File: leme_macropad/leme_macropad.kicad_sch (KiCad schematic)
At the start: 41 parts, among them J1 USB_C_Receptacle_USB2.0_16P, U1 SRV05-4HTG-D, U2 NCP1117-3.3_SOT223

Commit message: Changes resistors and capacitors to 0402
This should make it much easier to route things and to comply with the
signal integrity needs of some parts of the circuit.
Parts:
- C1, C2: footprint Capacitor_SMD:C_0603_1608Metric_Pad1.08x0.95mm_HandSolder -> Capacitor_SMD:C_0402_1005Metric_Pad0.74x0.62mm_HandSolder
- R1, R2: footprint Resistor_SMD:R_0603_1608Metric_Pad0.98x0.95mm_HandSolder -> Resistor_SMD:R_0402_1005Metric_Pad0.72x0.64mm_HandSolder
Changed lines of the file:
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@@
 			)
 		)
-		(property "Footprint" "Resistor_SMD:R_0603_1608Metric_Pad0.98x0.95mm_HandSolder"
+		(property "Footprint" "Resistor_SMD:R_0402_1005Metric_Pad0.72x0.64mm_HandSolder"
 			(at 54.61 43.18 0)
 			(effects
@@
 			)
 		)
-		(property "Footprint" "Capacitor_SMD:C_0603_1608Metric_Pad1.08x0.95mm_HandSolder"
+		(property "Footprint" "Capacitor_SMD:C_0402_1005Metric_Pad0.74x0.62mm_HandSolder"
 			(at 156.21 38.1 0)
 			(effects
@@
 			)
 		)
-		(property "Footprint" "Capacitor_SMD:C_0603_1608Metric_Pad1.08x0.95mm_HandSolder"
+		(property "Footprint" "Capacitor_SMD:C_0402_1005Metric_Pad0.74x0.62mm_HandSolder"
 			(at 125.73 38.1 0)
 			(effects
@@
 			)
 		)
-		(property "Footprint" "Resistor_SMD:R_0603_1608Metric_Pad0.98x0.95mm_HandSolder"
+		(property "Footprint" "Resistor_SMD:R_0402_1005Metric_Pad0.72x0.64mm_HandSolder"
 			(at 54.61 40.64 0)
 			(effects

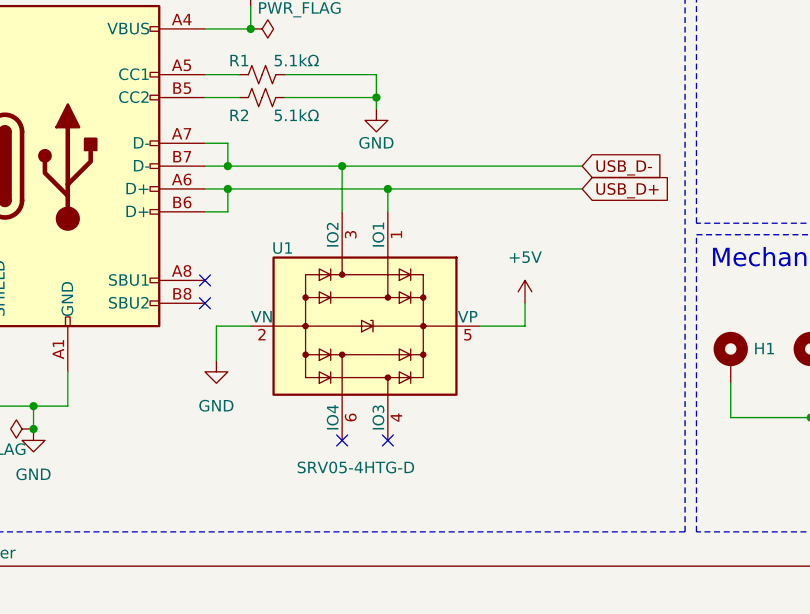
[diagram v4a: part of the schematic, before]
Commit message: Swaps USB pins on SRV05 to make routing easier
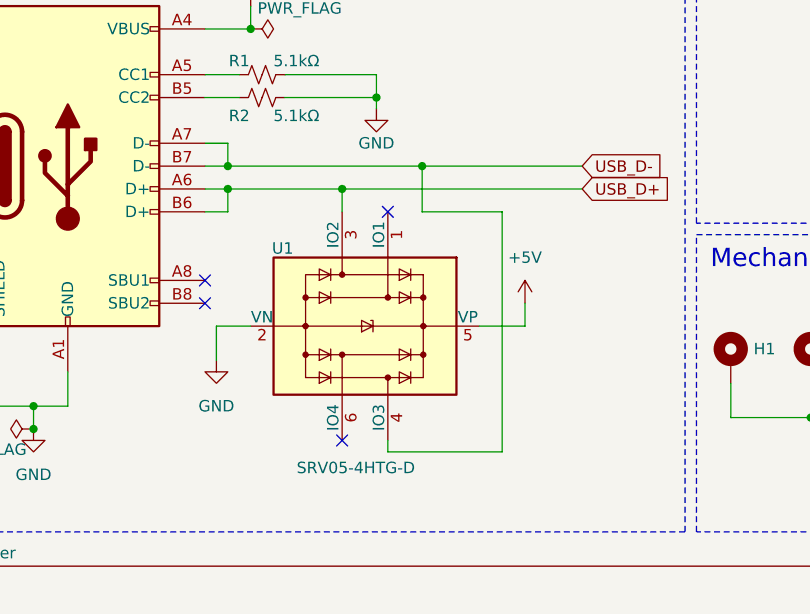
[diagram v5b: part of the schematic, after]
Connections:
- net USB_D+: now also U1.3 (IO2); no longer U1.1 (IO1)
- net USB_D-: now also U1.4 (IO3); no longer U1.3 (IO2)
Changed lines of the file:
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@@
 	)
 	(junction
-		(at 68.58 53.34)
+		(at 63.5 53.34)
 		(diameter 0)
 		(color 0 0 0 0)
@@
 	)
 	(junction
+		(at 72.39 50.8)
+		(diameter 0)
+		(color 0 0 0 0)
+	)
+	(junction
 		(at 53.34 35.56)
 		(diameter 0)
@@
 	)
 	(junction
-		(at 63.5 50.8)
-		(diameter 0)
-		(color 0 0 0 0)
-	)
-	(junction
 		(at 120.65 78.74)
 		(diameter 0)
@@
 	)
 	(no_connect
-		(at 68.58 81.28)
-	)
-	(no_connect
 		(at 48.26 66.04)
 	)
@@
 		(at 48.26 63.5)
 	)
+	(no_connect
+		(at 68.58 55.88)
+	)
 	(wire
 		(pts
@@
 	(wire
 		(pts
-			(xy 63.5 50.8) (xy 63.5 55.88)
-		)
-		(stroke
-			(width 0)
-			(type default)
-		)
-	)
-	(wire
-		(pts
 			(xy 166.37 163.83) (xy 166.37 168.91)
 		)
@@
 	(wire
 		(pts
-			(xy 63.5 50.8) (xy 90.17 50.8)
+			(xy 81.28 55.88) (xy 72.39 55.88)
 		)
 		(stroke
@@
 	(wire
 		(pts
+			(xy 68.58 82.55) (xy 81.28 82.55)
+		)
+		(stroke
+			(width 0)
+			(type default)
+		)
+	)
+	(wire
+		(pts
 			(xy 125.73 78.74) (xy 120.65 78.74)
 		)
@@
 	(wire
 		(pts
+			(xy 63.5 53.34) (xy 90.17 53.34)
+		)
+		(stroke
+			(width 0)
+			(type default)
+		)
+	)
+	(wire
+		(pts
 			(xy 49.53 68.58) (xy 53.34 68.58)
 		)
@@
 	(wire
 		(pts
+			(xy 63.5 53.34) (xy 63.5 55.88)
+		)
+		(stroke
+			(width 0)
+			(type default)
+		)
+	)
+	(wire
+		(pts
 			(xy 127 180.34) (xy 123.19 180.34)
 		)
@@
 	(wire
 		(pts
-			(xy 50.8 53.34) (xy 68.58 53.34)
+			(xy 50.8 53.34) (xy 63.5 53.34)
 		)
 		(stroke
@@
 	(wire
 		(pts
+			(xy 68.58 81.28) (xy 68.58 82.55)
+		)
+		(stroke
+			(width 0)
+			(type default)
+		)
+	)
+	(wire
+		(pts
 			(xy 156.21 163.83) (xy 156.21 168.91)
 		)
@@
 	(wire
 		(pts
-			(xy 68.58 53.34) (xy 90.17 53.34)
+			(xy 81.28 82.55) (xy 81.28 55.88)
+		)
+		(stroke
+			(width 0)
+			(type default)
+		)
+	)
+	(wire
+		(pts
+			(xy 72.39 50.8) (xy 72.39 55.88)
 		)
 		(stroke
@@
 	(wire
 		(pts
+			(xy 72.39 50.8) (xy 90.17 50.8)
+		)
+		(stroke
+			(width 0)
+			(type default)
+		)
+	)
+	(wire
+		(pts
 			(xy 29.21 80.01) (xy 29.21 77.47)
 		)
@@
 	(wire
 		(pts
-			(xy 50.8 50.8) (xy 63.5 50.8)
-		)
-		(stroke
-			(width 0)
-			(type default)
-		)
-	)
-	(wire
-		(pts
-			(xy 68.58 53.34) (xy 68.58 55.88)
-		)
-		(stroke
+			(xy 50.8 50.8) (xy 72.39 50.8)
+		)
+		(stroke

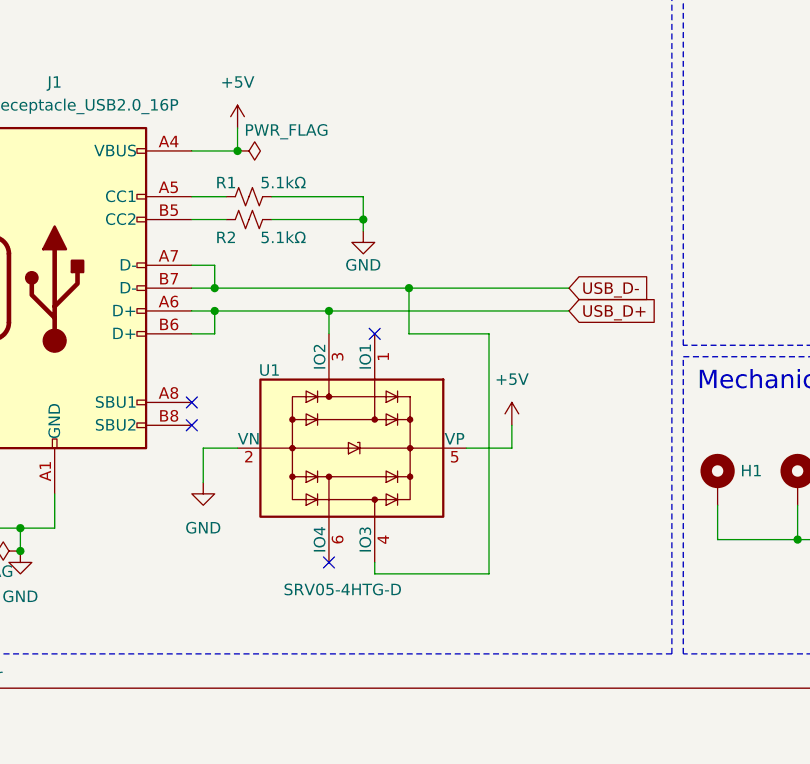
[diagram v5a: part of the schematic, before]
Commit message: Replaces SRV05 with USBLC6 for ESD protection
The USBLC6 is not only built specifically to protect USB data lines, but
is also cheaper than the SRV05.
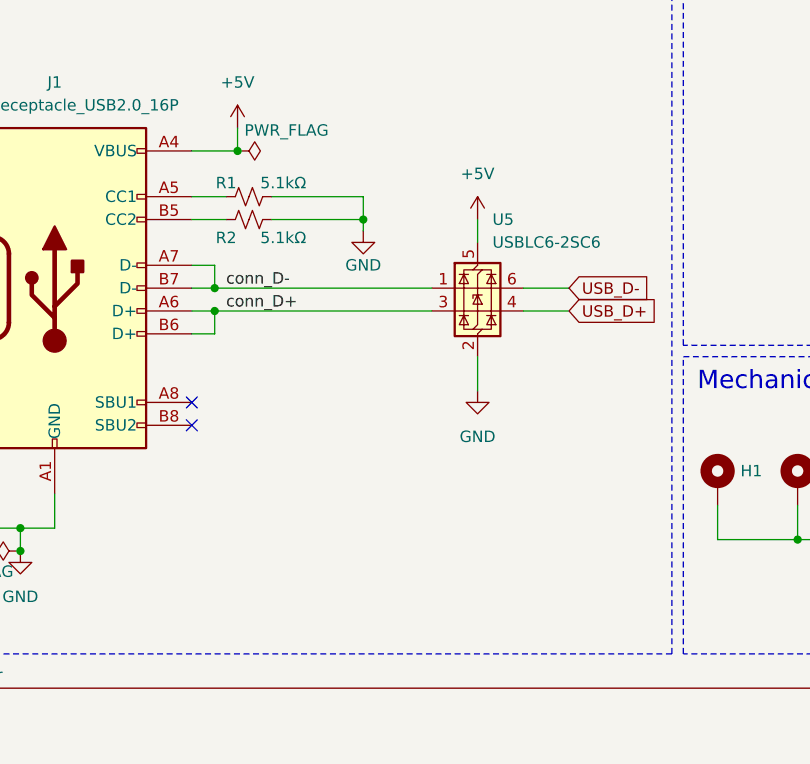
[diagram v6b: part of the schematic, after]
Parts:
- removed U1: SRV05-4HTG-D, Package_TO_SOT_SMD:SOT-23-6, symbol Power_Protection:SRV05-4
- added U5: USBLC6-2SC6, Package_TO_SOT_SMD:SOT-23-6, symbol Power_Protection:USBLC6-2SC6
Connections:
- net +5V: now also U5.5 (VBUS)
- net GND: now also U5.2 (GND)
- net USB_D+: now also U5.4 (I/O2); no longer J1.A6 (D+), J1.B6 (D+)
- net USB_D-: now also U5.6 (I/O1); no longer J1.A7 (D-), J1.B7 (D-)
- new net conn_D+: J1.A6 (D+), J1.B6 (D+), U5.3 (I/O2)
- new net conn_D-: J1.A7 (D-), J1.B7 (D-), U5.1 (I/O1)
- no-connect marks 4 -> 2

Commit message: Roughly positions logo
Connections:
- net GND: no longer GL1.1
- no-connect marks 2 -> 3
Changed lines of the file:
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@@
 		(at 48.26 63.5)
 	)
+	(no_connect
+		(at 157.48 83.82)
+	)
 	(wire
 		(pts
@@
 					(unit 1)
 				)
-			)
-		)
-	)
-	(symbol
-		(lib_id "power:GND")
-		(at 157.48 83.82 0)
-		(unit 1)
-		(exclude_from_sim no)
-		(in_bom yes)
-		(on_board yes)
-		(dnp no)
-		(fields_autoplaced yes)
-		(property "Reference" "#PWR062"
-			(at 157.48 90.17 0)
-			(effects
-				(font
-					(size 1.27 1.27)
-				)
-				(hide yes)
-			)
-		)
-		(property "Value" "GND"
-			(at 157.48 88.9 0)
-			(effects
-				(font
-					(size 1.27 1.27)
-				)
-			)
-		)
-		(property "Footprint" ""
-			(at 157.48 83.82 0)
-			(effects
-				(font
-					(size 1.27 1.27)
-				)
-				(hide yes)
-			)
-		)
-		(property "Datasheet" ""
-			(at 157.48 83.82 0)
-			(effects
-				(font
-					(size 1.27 1.27)
-				)
-				(hide yes)
-			)
-		)
-		(property "Description" "Power symbol creates a global label with name \"GND\" , ground"
-			(at 157.48 83.82 0)
-			(effects
-				(font
-					(size 1.27 1.27)
-				)
-				(hide yes)
-			)
-		)
-		(pin "1"
-		)
-		(instances
-			(project "leme_macropad"
-				(path "/a37365a2-c635-4451-9354-78f9e753d687"
-					(reference "#PWR062")
-					(unit 1)
-				)

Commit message: Use smaller testpoint pads
We have quite a few of them, and at 2mm it was impossible to space them
0.1" apart.
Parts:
- TP1, TP10, TP11, TP12, TP13, TP14, TP15, TP16, TP17, TP18, TP19, TP2, TP20, TP21, TP22, TP23, TP24, TP25, TP26, TP27, TP28, TP29, TP3, TP4, TP5, TP6, TP7, TP8, TP9: footprint TestPoint:TestPoint_Pad_D2.0mm -> TestPoint:TestPoint_Pad_D1.0mm
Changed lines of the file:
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@@
 			)
 		)
-		(property "Footprint" "TestPoint:TestPoint_Pad_D2.0mm"
+		(property "Footprint" "TestPoint:TestPoint_Pad_D1.0mm"
 			(at 88.9 179.07 0)
 			(effects
@@
 			)
 		)
-		(property "Footprint" "TestPoint:TestPoint_Pad_D2.0mm"
+		(property "Footprint" "TestPoint:TestPoint_Pad_D1.0mm"
 			(at 88.9 160.02 0)
 			(effects
@@
 			)
 		)
-		(property "Footprint" "TestPoint:TestPoint_Pad_D2.0mm"
+		(property "Footprint" "TestPoint:TestPoint_Pad_D1.0mm"
 			(at 54.61 161.29 0)
 			(effects
@@
 			)
 		)
-		(property "Footprint" "TestPoint:TestPoint_Pad_D2.0mm"
+		(property "Footprint" "TestPoint:TestPoint_Pad_D1.0mm"
 			(at 161.29 168.91 0)
 			(effects
@@
 			)
 		)
-		(property "Footprint" "TestPoint:TestPoint_Pad_D2.0mm"
+		(property "Footprint" "TestPoint:TestPoint_Pad_D1.0mm"
 			(at 22.86 175.26 0)
 			(effects
@@
 			)
 		)
-		(property "Footprint" "TestPoint:TestPoint_Pad_D2.0mm"
+		(property "Footprint" "TestPoint:TestPoint_Pad_D1.0mm"
 			(at 54.61 182.88 0)
 			(effects
@@
 			)
 		)
-		(property "Footprint" "TestPoint:TestPoint_Pad_D2.0mm"
+		(property "Footprint" "TestPoint:TestPoint_Pad_D1.0mm"
 			(at 88.9 163.83 0)
 			(effects
@@
 			)
 		)
-		(property "Footprint" "TestPoint:TestPoint_Pad_D2.0mm"
+		(property "Footprint" "TestPoint:TestPoint_Pad_D1.0mm"
 			(at 54.61 179.07 0)
 			(effects
@@
 			)
 		)
-		(property "Footprint" "TestPoint:TestPoint_Pad_D2.0mm"
+		(property "Footprint" "TestPoint:TestPoint_Pad_D1.0mm"
 			(at 54.61 173.99 0)
 			(effects
@@
 			)
 		)
-		(property "Footprint" "TestPoint:TestPoint_Pad_D2.0mm"
+		(property "Footprint" "TestPoint:TestPoint_Pad_D1.0mm"
 			(at 88.9 167.64 0)
 			(effects
@@
 			)
 		)
-		(property "Footprint" "TestPoint:TestPoint_Pad_D2.0mm"
+		(property "Footprint" "TestPoint:TestPoint_Pad_D1.0mm"
 			(at 123.19 160.02 0)
 			(effects
@@
 			)
 		)
-		(property "Footprint" "TestPoint:TestPoint_Pad_D2.0mm"
+		(property "Footprint" "TestPoint:TestPoint_Pad_D1.0mm"
 			(at 175.26 185.42 0)
 			(effects
@@
 			)
 		)
-		(property "Footprint" "TestPoint:TestPoint_Pad_D2.0mm"
+		(property "Footprint" "TestPoint:TestPoint_Pad_D1.0mm"
 			(at 54.61 170.18 0)
 			(effects
@@
 			)
 		)
-		(property "Footprint" "TestPoint:TestPoint_Pad_D2.0mm"
+		(property "Footprint" "TestPoint:TestPoint_Pad_D1.0mm"
 			(at 123.19 167.64 0)
 			(effects
@@
 			)
 		)
-		(property "Footprint" "TestPoint:TestPoint_Pad_D2.0mm"
+		(property "Footprint" "TestPoint:TestPoint_Pad_D1.0mm"
 			(at 88.9 175.26 0)
 			(effects
@@
 			)
 		)
-		(property "Footprint" "TestPoint:TestPoint_Pad_D2.0mm"
+		(property "Footprint" "TestPoint:TestPoint_Pad_D1.0mm"
 			(at 54.61 165.1 0)
 			(effects
@@
 			)
 		)
-		(property "Footprint" "TestPoint:TestPoint_Pad_D2.0mm"
+		(property "Footprint" "TestPoint:TestPoint_Pad_D1.0mm"
 			(at 88.9 182.88 0)
 			(effects
@@
 			)
 		)
-		(property "Footprint" "TestPoint:TestPoint_Pad_D2.0mm"
+		(property "Footprint" "TestPoint:TestPoint_Pad_D1.0mm"
 			(at 123.19 182.88 0)
 			(effects
@@
 			)
 		)
-		(property "Footprint" "TestPoint:TestPoint_Pad_D2.0mm"
+		(property "Footprint" "TestPoint:TestPoint_Pad_D1.0mm"
 			(at 123.19 156.21 0)
 			(effects
@@
 			)
 		)
-		(property "Footprint" "TestPoint:TestPoint_Pad_D2.0mm"
+		(property "Footprint" "TestPoint:TestPoint_Pad_D1.0mm"
 			(at 123.19 179.07 0)
 			(effects
@@
 			)
 		)
-		(property "Footprint" "TestPoint:TestPoint_Pad_D2.0mm"
+		(property "Footprint" "TestPoint:TestPoint_Pad_D1.0mm"
 			(at 157.48 185.42 0)
 			(effects
@@
 			)
 		)
-		(property "Footprint" "TestPoint:TestPoint_Pad_D2.0mm"
+		(property "Footprint" "TestPoint:TestPoint_Pad_D1.0mm"
 			(at 151.13 168.91 0)
 			(effects
@@
 			)
 		)
-		(property "Footprint" "TestPoint:TestPoint_Pad_D2.0mm"
+		(property "Footprint" "TestPoint:TestPoint_Pad_D1.0mm"
 			(at 22.86 182.88 0)
 			(effects
@@
 			)
 		)
-		(property "Footprint" "TestPoint:TestPoint_Pad_D2.0mm"
+		(property "Footprint" "TestPoint:TestPoint_Pad_D1.0mm"
 			(at 22.86 179.07 0)
 			(effects
@@
 			)
 		)
-		(property "Footprint" "TestPoint:TestPoint_Pad_D2.0mm"
+		(property "Footprint" "TestPoint:TestPoint_Pad_D1.0mm"
 			(at 123.19 171.45 0)
 			(effects
@@
 			)
 		)
-		(property "Footprint" "TestPoint:TestPoint_Pad_D2.0mm"
+		(property "Footprint" "TestPoint:TestPoint_Pad_D1.0mm"
 			(at 88.9 171.45 0)
 			(effects
@@
 			)
 		)
-		(property "Footprint" "TestPoint:TestPoint_Pad_D2.0mm"
+		(property "Footprint" "TestPoint:TestPoint_Pad_D1.0mm"
 			(at 123.19 175.26 0)
 			(effects
@@
 			)
 		)
-		(property "Footprint" "TestPoint:TestPoint_Pad_D2.0mm"
+		(property "Footprint" "TestPoint:TestPoint_Pad_D1.0mm"
 			(at 166.37 185.42 0)
 			(effects
@@
 			)
 		)
-		(property "Footprint" "TestPoint:TestPoint_Pad_D2.0mm"
+		(property "Footprint" "TestPoint:TestPoint_Pad_D1.0mm"
 			(at 88.9 156.21 0)
 			(effects
